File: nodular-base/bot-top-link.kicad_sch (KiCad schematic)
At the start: 21 parts, among them J9 Conn_01x30_MountingPin, U13 MT9700, U17 RCLAMP0524P-ES, U6 74LVC1G17

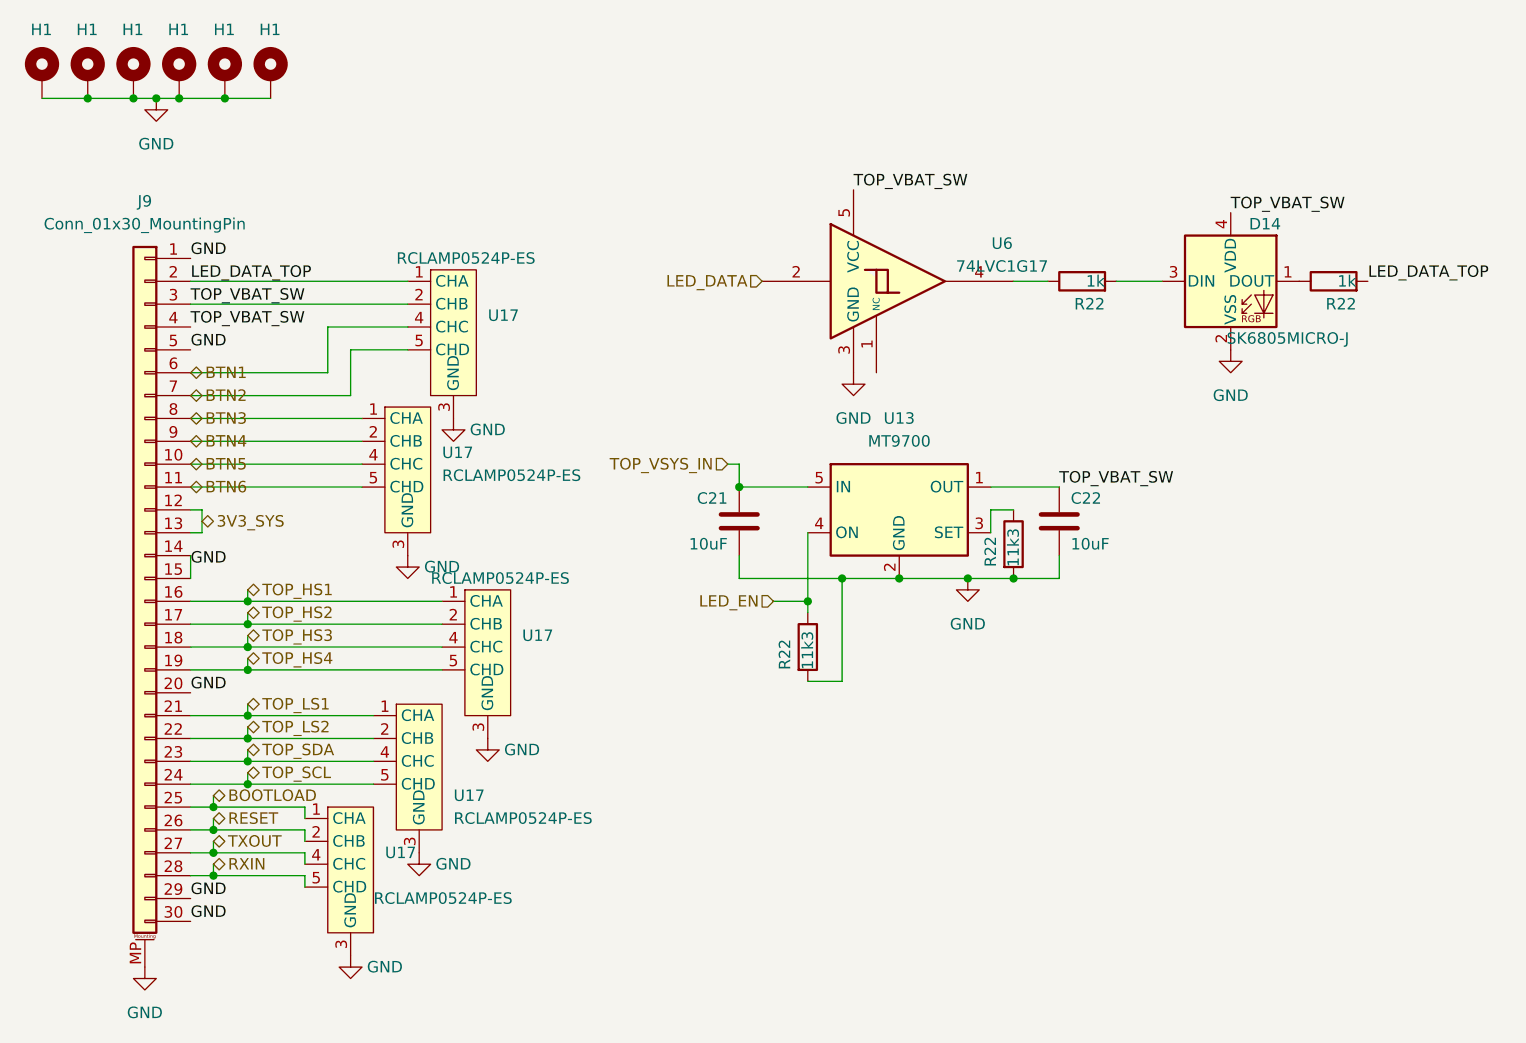
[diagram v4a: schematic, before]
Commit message: Modify base board: - Fix ESP32 strapping pins state - Remove 3/6 M3 standoffs - Change to LGA-style pads on ESP32 - Modify SFP mechanical pads to not be plated - Add larger mechanical pads with more solder paste surface to USB-C connectors
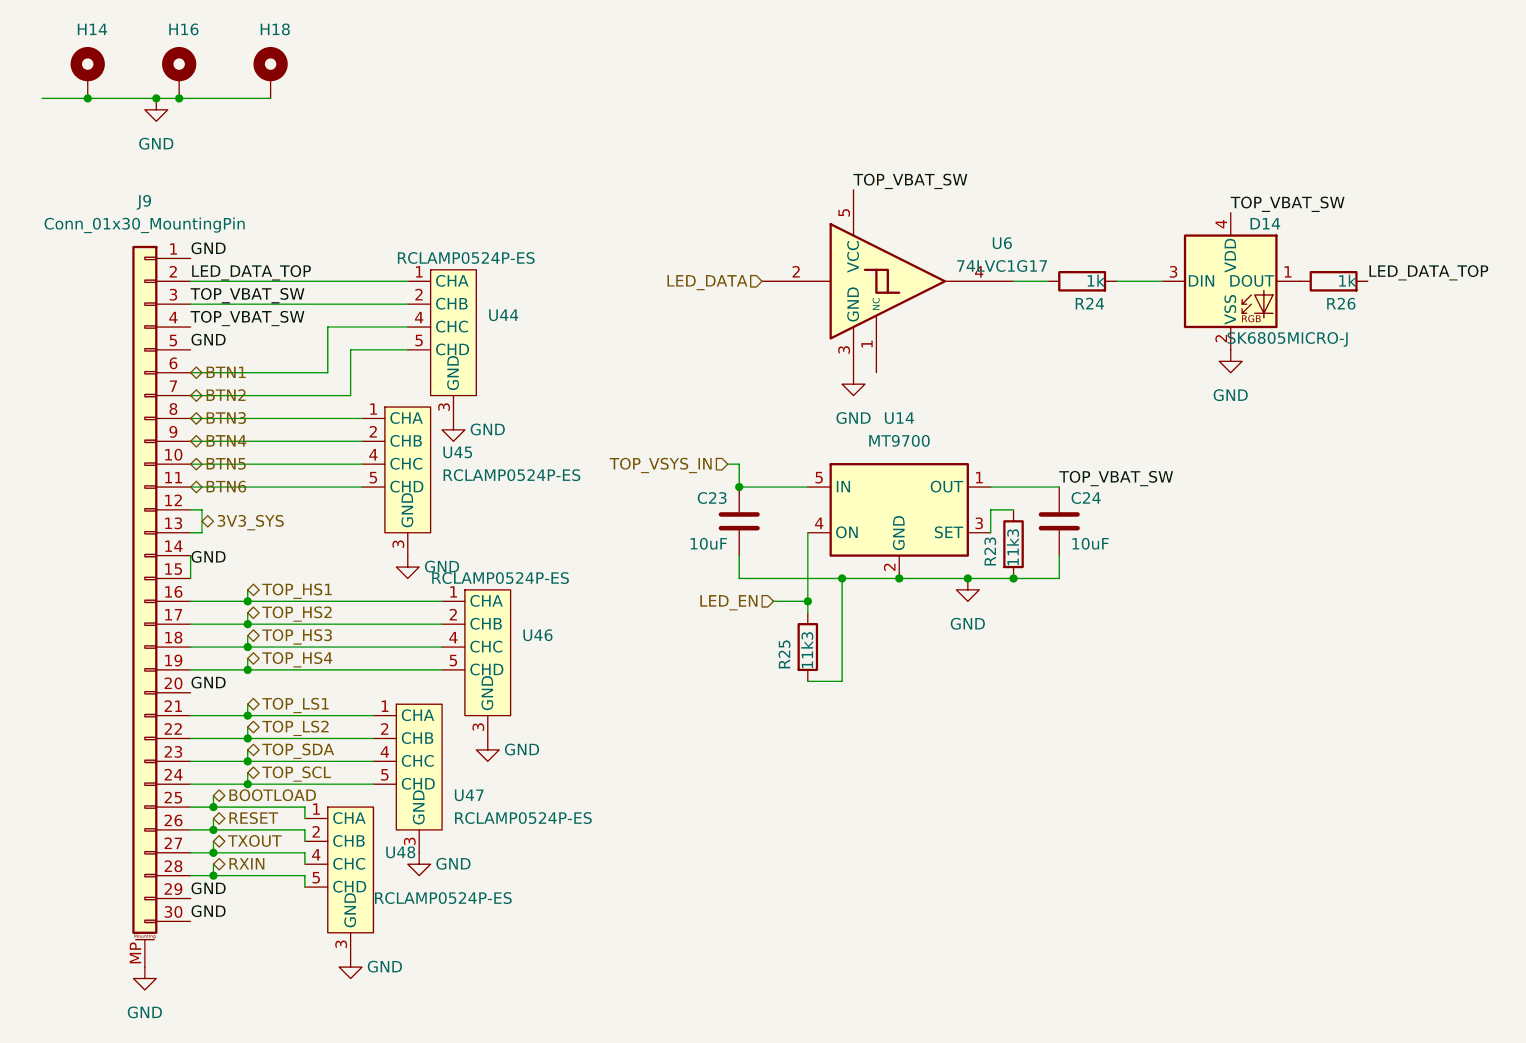
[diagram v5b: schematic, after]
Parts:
- removed H1 (x3): MountingHole_Pad, nodular:SMTSO3030CTJ, symbol Mechanical:MountingHole_Pad
- renumbered C21 to C23, C22 to C24, H1 to H14, H1 to H16, H1 to H18, R22 to R23, R22 to R24, R22 to R25, R22 to R26, U13 to U14, U17 to U44, U17 to U45, U17 to U46, U17 to U47, U17 to U48
